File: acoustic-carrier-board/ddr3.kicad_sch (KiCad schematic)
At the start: 77 parts, among them IC1101 MT41K256M16TW-107_P

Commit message: Modified README, lpddr3 testpoint search
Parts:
- TP1149: footprint iw-misc:TestPoint_Pad_D0.25mm -> iw-misc:TestPoint_Pad_D0.125mm
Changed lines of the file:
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@@
 			)
 		)
-		(property "Footprint" "iw-misc:TestPoint_Pad_D0.25mm"
+		(property "Footprint" "iw-misc:TestPoint_Pad_D0.125mm"
 			(at 44.45 124.46 0)
 			(effects
@@
 			(effects
 				(font
-					(size 1.27 1.27)
-				)
-				(hide yes)
-			)
-		)
-		(property "Availability" ""
-			(at 189.23 40.64 0)
-			(effects
-				(font
-					(size 1.27 1.27)
-				)
-				(hide yes)
-			)
-		)
-		(property "Check_prices" ""
-			(at 189.23 40.64 0)
-			(effects
-				(font

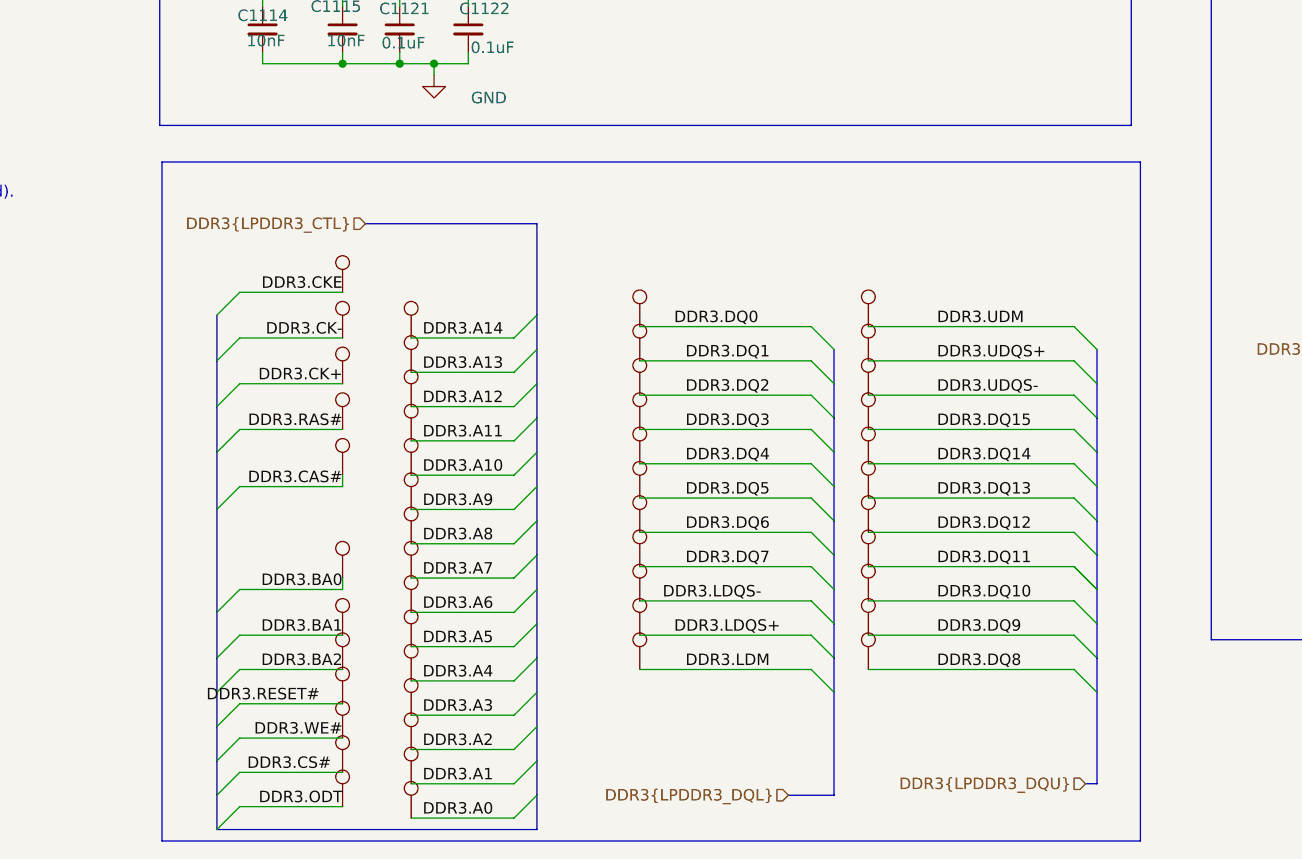
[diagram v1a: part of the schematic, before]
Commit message: Modified readme, removed testpoints and stubs, changed simulation folder structure, removed excess length matching
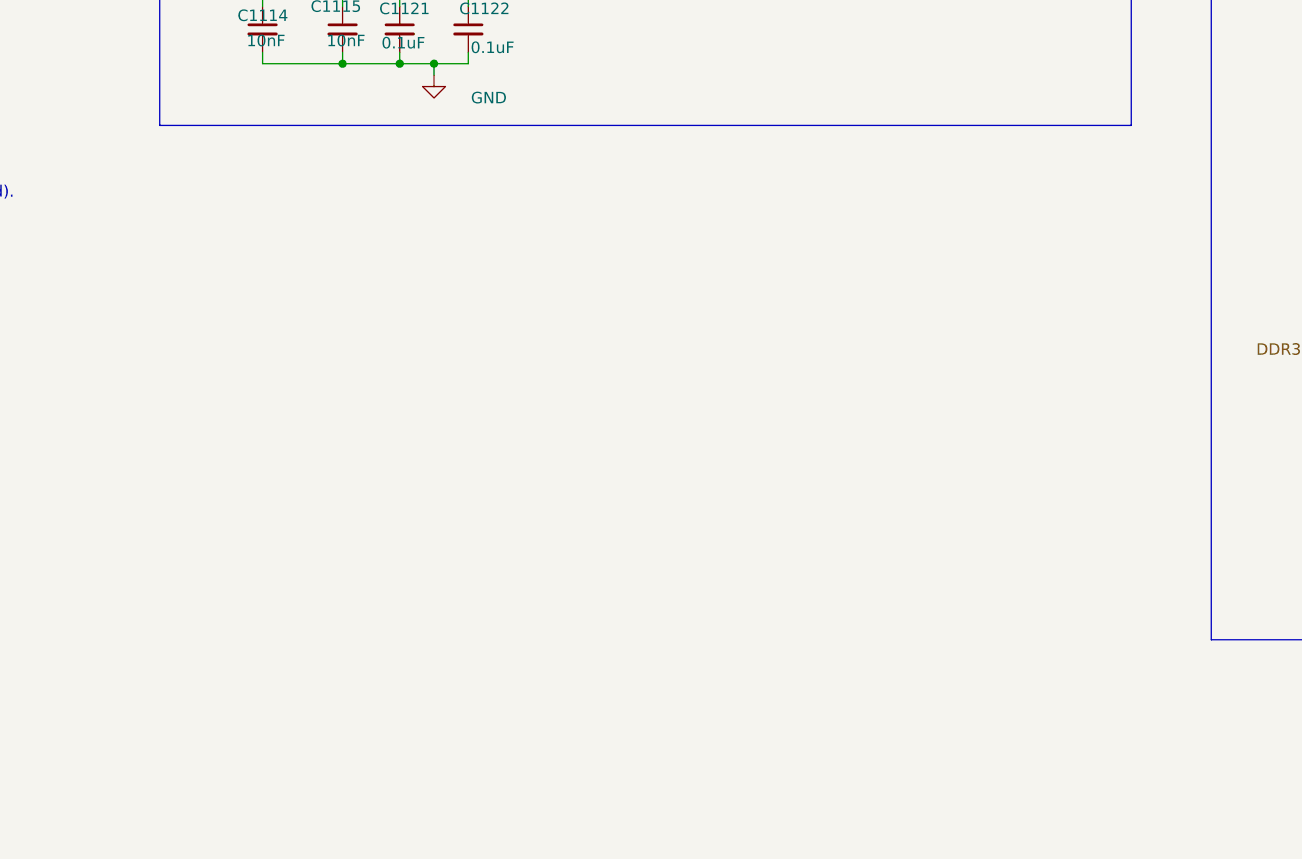
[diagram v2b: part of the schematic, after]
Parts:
- removed TP1101, TP1102, TP1103, TP1104, TP1105, TP1106, TP1107, TP1108, TP1109, TP1110, TP1111, TP1112, TP1113, TP1114, TP1115, TP1116, TP1117, TP1118, TP1119, TP1120, TP1121, TP1122, TP1123, TP1124, TP1125, TP1126, TP1127, TP1128, TP1129, TP1130, TP1131, TP1132, TP1133, TP1134, TP1135, TP1136, TP1137, TP1138, TP1139, TP1140, TP1141, TP1142, TP1143, TP1144, TP1145, TP1146, TP1147, TP1148: TestPoint_0.25mm, iw-misc:TestPoint_Pad_D0.25mm, symbol iw-misc:TestPoint_0.25mm
- removed TP1149: TestPoint_0.25mm, iw-misc:TestPoint_Pad_D0.125mm, symbol iw-misc:TestPoint_0.25mm

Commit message: added step-files
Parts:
- C1101, C1102, C1103, C1104, C1105, C1106, C1108, C1109, C1110, C1111, C1112, C1116, C1118, C1119, C1120, C1121, C1122, C1123, C1124, C1125: LCSC Part Number (none) -> C22435929; LPN C22435929 -> (none); MPN CGA0201X7R104K160ET -> (none); Manufacturing Part Number (none) -> CGA0201X7R104K160ET
- C1107, C1113: LCSC Part Number (none) -> C59461; LPN C59461 -> (none); MPN CL10A226MQ8NRNC -> (none); Manufacturing Part Number (none) -> CL10A226MQ8NRNC
- C1114, C1115: LCSC Part Number (none) -> C285010; LPN C285010 -> (none); MPN 0201B103K250NT -> (none); Manufacturing Part Number (none) -> 0201B103K250NT
- IC1101: LCSC Part Number (none) -> C253882; LPN C253882 -> (none); MPN MT41K256M16TW-107:P -> (none); Manufacturing Part Number (none) -> MT41K256M16TW-107:P
- L1101, L1102: LCSC Part Number (none) -> C113030; LPN C113030 -> (none); MPN BLM18SG121TN1D -> (none); Manufacturing Part Number (none) -> BLM18SG121TN1D
- R1101: LCSC Part Number (none) -> C23350; LPN C23350 -> (none); MPN 0603WAF2400T5E -> (none); Manufacturing Part Number (none) -> 0603WAF2400T5E

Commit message: order carrier board
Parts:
- L1101, L1102: LCSC Part Number C113030 -> C285595; Manufacturing Part Number BLM18SG121TN1D -> UPB160805T-121Y-N
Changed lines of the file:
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@@
 			)
 		)
-		(property "LCSC Part Number" "C113030"
+		(property "LCSC Part Number" "C285595"
 			(at 36.83 59.69 90)
 			(effects
@@
 			)
 		)
-		(property "Manufacturing Part Number" "BLM18SG121TN1D"
+		(property "Manufacturing Part Number" "UPB160805T-121Y-N "
 			(at 36.83 59.69 90)
 			(effects
@@
 			)
 		)
-		(property "LCSC Part Number" "C113030"
+		(property "LCSC Part Number" "C285595"
 			(at 39.37 24.13 90)
 			(effects
@@
 			)
 		)
-		(property "Manufacturing Part Number" "BLM18SG121TN1D"
+		(property "Manufacturing Part Number" "UPB160805T-121Y-N "
 			(at 39.37 24.13 90)
 			(effects
